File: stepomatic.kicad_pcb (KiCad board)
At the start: 2 copper layers, 50 x 30 mm, 31 parts, among them J1 I2C, J2 Conn_01x05, J4 USB_B_Micro, Q1 MMBT3904, Q2 MMBT3904, SW1 Mode, SW2 RST, U1 HDC1080DMBR, U2 AMS1117-3.3, U3 ULN2003A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

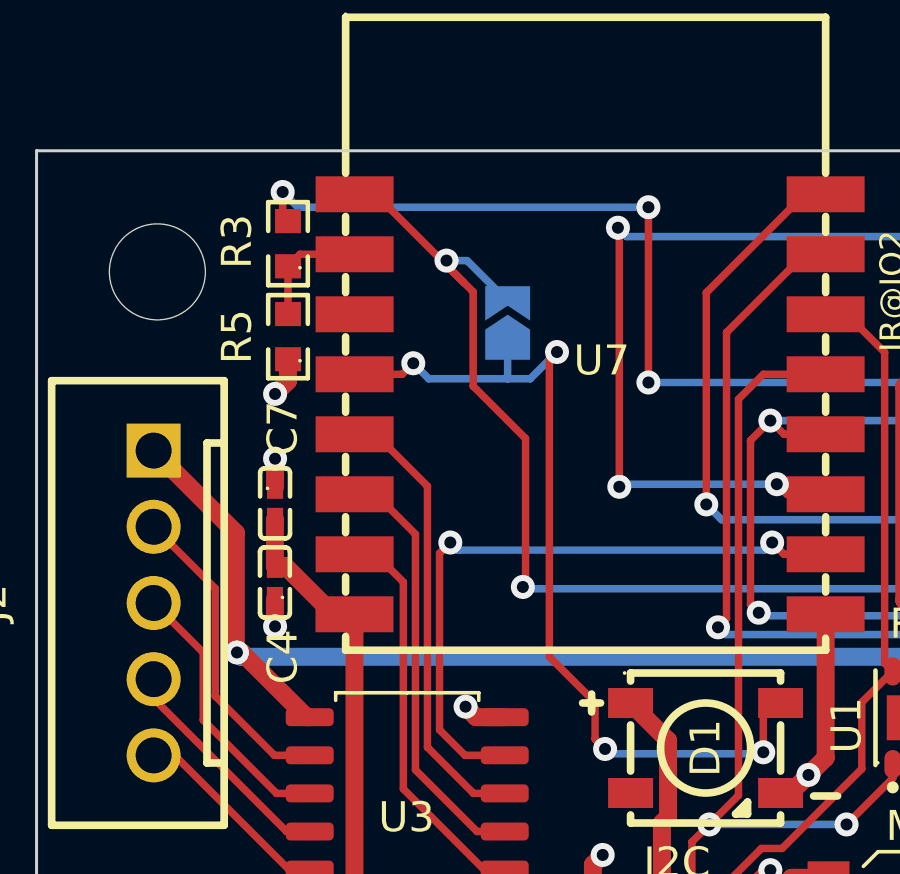
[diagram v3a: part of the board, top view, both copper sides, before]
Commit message: Fix package of C3
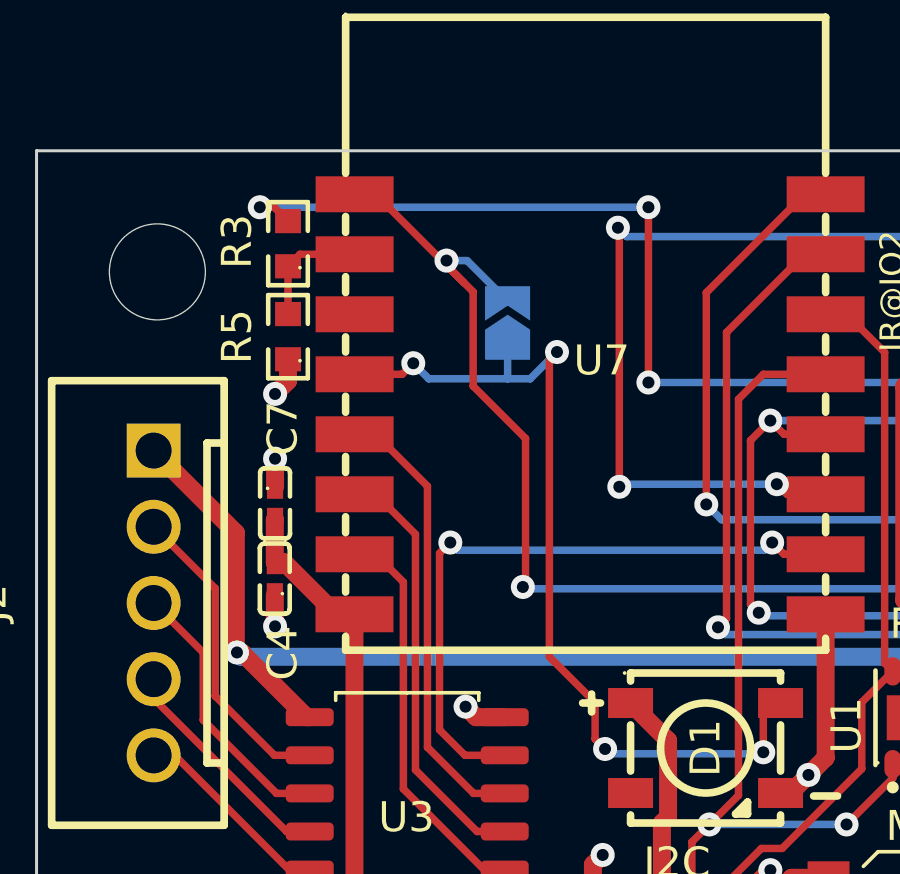
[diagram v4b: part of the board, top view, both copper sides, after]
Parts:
- moved C4 0.12 mm to (107.9, 84.3)
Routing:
- net Net-(CGQ1-Pad2): track 46.4 -> 47.1 mm
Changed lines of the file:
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@@
   )
   (footprint "footprint:C0402" (layer "F.Cu")
-    (at 107.94585 84.387329 90)
+    (at 107.941145 84.263232 90)
     (descr "C0402 footprint")
     (tags "C0402 footprint C1525")
@@
   (segment (start 141.475 86.8) (end 141.407 86.868) (width 0.6) (layer "B.Cu") (net 1))
   (segment (start 141.407 86.868) (end 106.824848 86.868) (width 0.6) (layer "B.Cu") (net 1))
-  (segment (start 107.94585 84.932414) (end 107.94585 85.84785) (width 0.6) (layer "F.Cu") (net 2))
   (segment (start 125.127358 91.407642) (end 125.73 90.805) (width 0.6) (layer "F.Cu") (net 2))
   (segment (start 133.33125 76.94325) (end 132.842 76.454) (width 0.6) (layer "F.Cu") (net 2))
@@
   (segment (start 132.6 94.234) (end 135.15 94.234) (width 0.6) (layer "F.Cu") (net 2))
   (segment (start 148.564985 78.627006) (end 148.564985 85.627006) (width 0.6) (layer "F.Cu") (net 2))
+  (segment (start 107.941145 84.808317) (end 107.941145 85.843145) (width 0.6) (layer "F.Cu") (net 2))
   (segment (start 143.346113 91.592136) (end 143.153977 91.4) (width 0.6) (layer "F.Cu") (net 2))
   (segment (start 141.35 94.234) (end 140.208 94.234) (width 0.6) (layer "F.Cu") (net 2))
@@
   (segment (start 145.864985 79.627006) (end 145.864985 80.677504) (width 0.6) (layer "F.Cu") (net 2))
   (segment (start 131.41617 76.454) (end 132.292049 76.454) (width 0.6) (layer "F.Cu") (net 2))
-  (segment (start 107.94585 85.84785) (end 107.95 85.852) (width 0.6) (layer "F.Cu") (net 2))
   (segment (start 124.145413 96.834587) (end 123.952 97.028) (width 0.6) (layer "F.Cu") (net 2))
   (segment (start 134.334912 92.072942) (end 133.982942 92.072942) (width 0.6) (layer "F.Cu") (net 2))
@@
   (segment (start 134.742562 83.95105) (end 134.611512 83.82) (width 0.6) (layer "F.Cu") (net 2))
   (segment (start 134.611512 83.82) (end 134.112 83.82) (width 0.6) (layer "F.Cu") (net 2))
+  (segment (start 107.941145 85.843145) (end 107.95 85.852) (width 0.6) (layer "F.Cu") (net 2))
   (segment (start 133.982942 92.072942) (end 133.604 91.694) (width 0.6) (layer "F.Cu") (net 2))
   (segment (start 107.95 81.20583) (end 107.95 80.264) (width 0.6) (layer "F.Cu") (net 2))
@@
   (segment (start 134.62 78.232) (end 134.742562 78.109438) (width 0.6) (layer "F.Cu") (net 3))
   (segment (start 130.221998 78.232) (end 134.62 78.232) (width 0.6) (layer "F.Cu") (net 3))
-  (segment (start 108.28865 83.842244) (end 107.94585 83.842244) (width 0.6) (layer "F.Cu") (net 3))
   (segment (start 138.552562 82.672562) (end 138.552562 83.95105) (width 0.6) (layer "F.Cu") (net 3))
   (segment (start 137.046113 89.292136) (end 136.145977 88.392) (width 0.6) (layer "F.Cu") (net 3))
   (segment (start 128.922606 84.982065) (end 128.922606 77.857394) (width 0.6) (layer "F.Cu") (net 3))
   (segment (start 121.05133 89.657896) (end 119.80133 88.407896) (width 0.6) (layer "F.Cu") (net 3))
+  (segment (start 108.254961 83.718147) (end 107.941145 83.718147) (width 0.6) (layer "F.Cu") (net 3))
   (segment (start 129.3 72.784822) (end 129.3 76.44) (width 0.6) (layer "F.Cu") (net 3))
   (segment (start 134.742562 79.00105) (end 134.742562 80.06477) (width 0.6) (layer "F.Cu") (net 3))
   (segment (start 129.82 76.96) (end 129.82 77.830002) (width 0.6) (layer "F.Cu") (net 3))
   (segment (start 134.42142 77.289542) (end 134.742562 77.610684) (width 0.6) (layer "F.Cu") (net 3))
+  (segment (start 107.941145 82.304855) (end 107.95 82.296) (width 0.6) (layer "F.Cu") (net 3))
+  (segment (start 110.596431 85.450025) (end 109.986839 85.450025) (width 0.6) (layer "F.Cu") (net 3))
   (segment (start 140.275826 74.920003) (end 140.275826 76.334216) (width 0.6) (layer "F.Cu") (net 3))
   (segment (start 120.845438 92.407642) (end 121.05133 92.20175) (width 0.6) (layer "F.Cu") (net 3))
@@
   (segment (start 137.16 99.06) (end 137.668 98.552) (width 0.6) (layer "F.Cu") (net 3))
   (segment (start 120.845438 98.857516) (end 121.047922 99.06) (width 0.6) (layer "F.Cu") (net 3))
-  (segment (start 110.596431 85.450025) (end 109.896431 85.450025) (width 0.6) (layer "F.Cu") (net 3))
-  (segment (start 107.94585 83.842244) (end 107.94585 82.30015) (width 0.6) (layer "F.Cu") (net 3))
+  (segment (start 107.941145 83.718147) (end 107.941145 82.304855) (width 0.6) (layer "F.Cu") (net 3))
   (segment (start 120.845438 97.78251) (end 120.845438 92.407642) (width 0.6) (layer "F.Cu") (net 3))
   (segment (start 140.275826 76.334216) (end 139.083992 77.52605) (width 0.6) (layer "F.Cu") (net 3))
@@
   (segment (start 115.175863 99.06) (end 121.412 99.06) (width 0.6) (layer "F.Cu") (net 3))
   (segment (start 134.742562 77.610684) (end 134.742562 78.109438) (width 0.6) (layer "F.Cu") (net 3))
-  (segment (start 107.94585 82.30015) (end 107.95 82.296) (width 0.6) (layer "F.Cu") (net 3))
   (segment (start 139.083992 77.52605) (end 135.32595 77.52605) (width 0.6) (layer "F.Cu") (net 3))
   (segment (start 134.742562 78.109438) (end 134.742562 78.62347) (width 0.6) (layer "F.Cu") (net 3))
   (segment (start 138.552562 83.95105) (end 138.552562 87.785687) (width 0.6) (layer "F.Cu") (net 3))
   (segment (start 137.668 98.552) (end 137.668 89.914023) (width 0.6) (layer "F.Cu") (net 3))
+  (segment (start 109.986839 85.450025) (end 108.254961 83.718147) (width 0.6) (layer "F.Cu") (net 3))
   (segment (start 110.596431 85.450025) (end 110.596431 94.480568) (width 0.6) (layer "F.Cu") (net 3))
   (segment (start 129.779565 72.305257) (end 129.3 72.784822) (width 0.6) (layer "F.Cu") (net 3))
-  (segment (start 109.896431 85.450025) (end 108.28865 83.842244) (width 0.6) (layer "F.Cu") (net 3))
   (segment (start 103.902943 82.533519) (end 105.9555 84.586076) (width 0.25) (layer "F.Cu") (net 4))
   (segment (start 107.930543 90.150543) (end 109.105645 90.150543) (width 0.25) (layer "F.Cu") (net 4))
@@
   (segment (start 131.078016 73.421984) (end 131.078016 72.305257) (width 0.25) (layer "F.Cu") (net 47))
   (segment (start 130.55 73.95) (end 131.078016 73.421984) (width 0.25) (layer "F.Cu") (net 47))
+  (segment (start 107.920324 71.882) (end 107.442 71.882) (width 0.25) (layer "F.Cu") (net 48))
   (segment (start 120.396 77.724) (end 120.396 71.882) (width 0.25) (layer "F.Cu") (net 48))
   (segment (start 140.275826 72.379997) (end 141.732 73.836171) (width 0.25) (layer "F.Cu") (net 48))
-  (segment (start 108.204 72.165676) (end 108.38176 72.343436) (width 0.25) (layer "F.Cu") (net 48))
   (segment (start 141.732 73.836171) (end 141.732 77.47) (width 0.25) (layer "F.Cu") (net 48))
-  (segment (start 108.204 71.374) (end 108.204 72.165676) (width 0.25) (layer "F.Cu") (net 48))
+  (segment (start 108.38176 72.343436) (end 107.920324 71.882) (width 0.25) (layer "F.Cu") (net 48))
   (via (at 141.732 77.47) (size 0.8) (drill 0.4) (layers "F.Cu" "B.Cu") (net 48))
   (via (at 120.396 71.882) (size 0.8) (drill 0.4) (layers "F.Cu" "B.Cu") (net 48))
-  (via (at 108.204 71.374) (size 0.8) (drill 0.4) (layers "F.Cu" "B.Cu") (net 48))
+  (via (at 107.442 71.882) (size 0.8) (drill 0.4) (layers "F.Cu" "B.Cu") (net 48))
   (via (at 120.396 77.724) (size 0.8) (drill 0.4) (layers "F.Cu" "B.Cu") (net 48))
-  (segment (start 108.712 71.882) (end 108.204 71.374) (width 0.25) (layer "B.Cu") (net 48))
   (segment (start 141.478 77.724) (end 141.732 77.47) (width 0.25) (layer "B.Cu") (net 48))
-  (segment (start 120.396 71.882) (end 108.712 71.882) (width 0.25) (layer "B.Cu") (net 48))
+  (segment (start 120.396 71.882) (end 107.442 71.882) (width 0.25) (layer "B.Cu") (net 48))
   (segment (start 120.396 77.724) (end 141.478 77.724) (width 0.25) (layer "B.Cu") (net 48))
   (zone (net 3) (net_name "+3V3") (layer "F.Cu") (hatch edge 0.508)

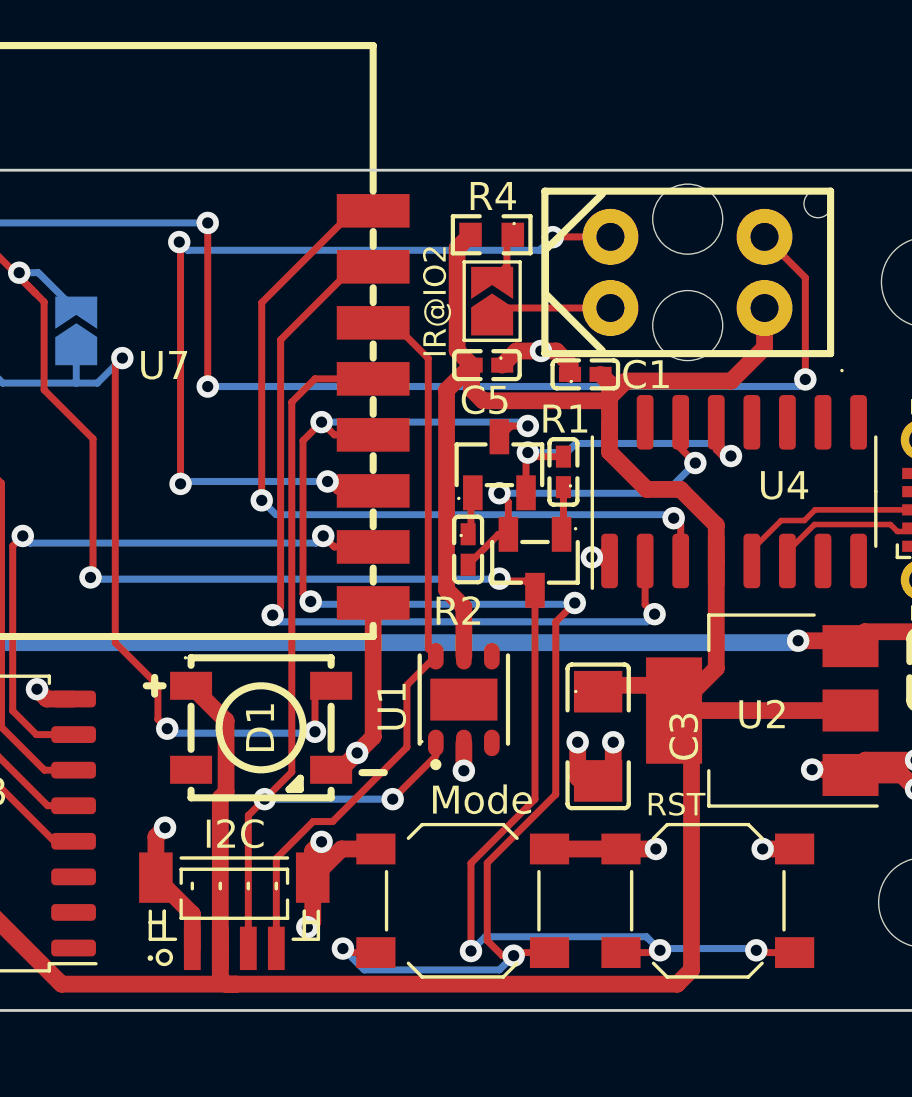
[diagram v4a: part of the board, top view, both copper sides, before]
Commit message: Allow to switch between ON and GPIO02 for IR send
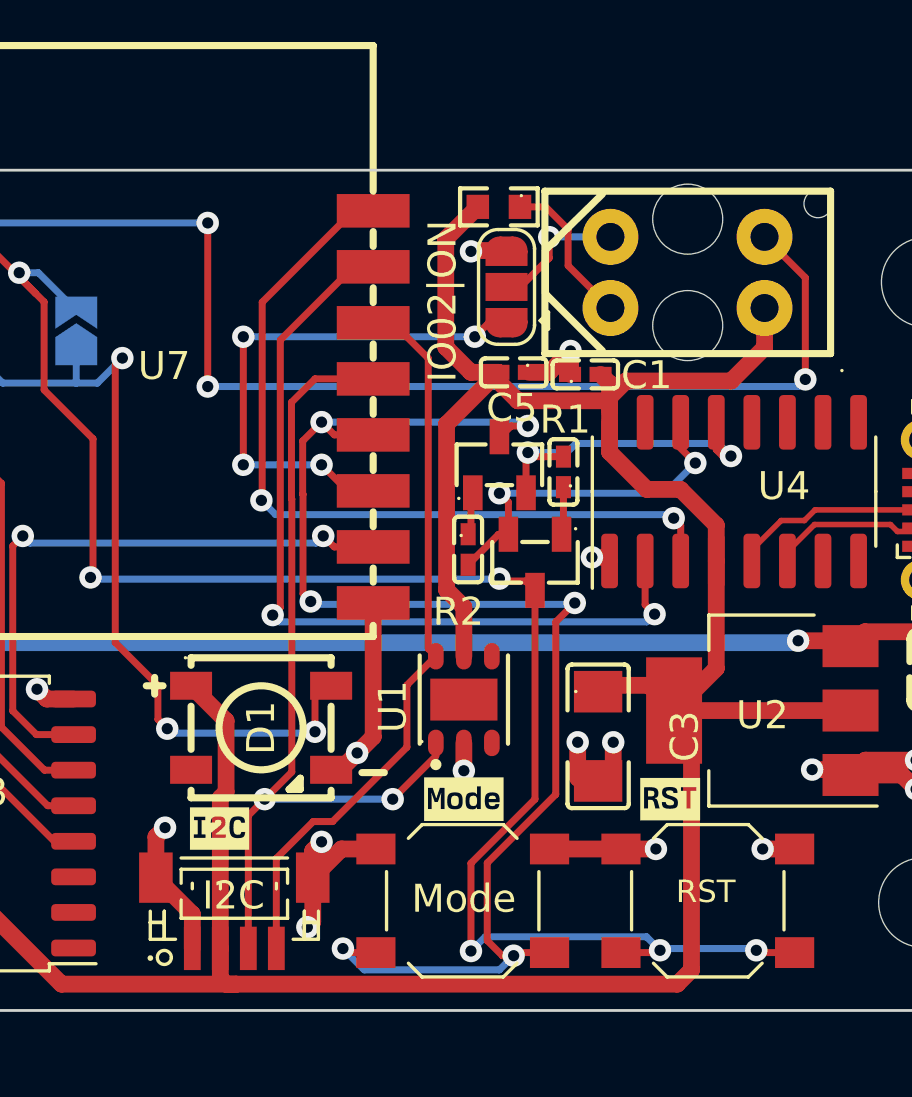
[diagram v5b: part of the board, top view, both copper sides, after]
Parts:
- added kibuzzard-65CA9226: G***, kibuzzard-65CA9226, F.Cu at (120.8, 93.5)
- added kibuzzard-65CA923B: G***, kibuzzard-65CA923B, F.Cu at (129.5, 92.5)
- added kibuzzard-65CA9256: G***, kibuzzard-65CA9256, F.Cu at (136.9, 92.5)
- JP2: value IR@IO2 -> IO02|ON; footprint Jumper:SolderJumper-2_P1.3mm_Open_TrianglePad1.0x1.5mm -> Jumper:SolderJumper-3_P1.3mm_Open_RoundedPad1.0x1.5mm
- moved R4 1.03 mm to (130.8, 71.3)
- moved C5 0.99 mm to (131.3, 77.2)
- moved JP2 0.72 mm to (131.1, 74.2)
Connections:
- CGQ1 pad 4: IR -> Net-(CGQ1-Pad4)
- JP2 pad 1: Net-(CGQ1-Pad3) -> IR
- JP2 pad 2: Net-(JP2-Pad2) -> Net-(CGQ1-Pad4)
- R4 pad 1: Net-(JP2-Pad2) -> Net-(CGQ1-Pad3)
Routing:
- net IR: track 31.4 -> 19.2 mm
- net Net-(CGQ1-Pad4): track 0.00 -> 4.89 mm, vias 0 -> 1
- net Net-(JP2-Pad2): track 1.86 -> 0.00 mm
- net +3V3: track 117.4 -> 118.8 mm
- net Net-(CGQ1-Pad3): track 4.42 -> 5.49 mm
- net GND: track 52.2 -> 53.0 mm, vias 19 -> 20
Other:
- board text added: "JLCJLCJLCJLC"

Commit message: Tidy up
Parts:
- added kibuzzard-65CA9AB8: G***, kibuzzard-65CA9AB8, F.Cu at (128.8, 74.4)
- added kibuzzard-65CA9B57: G***, kibuzzard-65CA9B57, F.Cu at (105.7, 76.7)
- added kibuzzard-65CA9BC7: G***, kibuzzard-65CA9BC7, B.Cu at (111.5, 75.7)
- added kibuzzard-65CA9C5F: G***, kibuzzard-65CA9C5F, F.Cu at (119.9, 99.1)
- added kibuzzard-65CA9C8E: G***, kibuzzard-65CA9C8E, F.Cu at (121.0, 99.1)
- added kibuzzard-65CA9CFD: G***, kibuzzard-65CA9CFD, F.Cu at (123.0, 99.1)
- added kibuzzard-65CA9D0A: G***, kibuzzard-65CA9D0A, F.Cu at (122.0, 99.1)
- added kibuzzard-65CA9D34: G***, kibuzzard-65CA9D34, F.Cu at (148.6, 88.4)
- added kibuzzard-65CA9DAF: G***, kibuzzard-65CA9DAF, F.Cu at (103.4, 93.3)
- J2: value Conn_01x05 -> 28BYJ-48
- JP2: value IO02|ON -> IR
- moved kibuzzard-65CA9256 0.76 mm to (137.7, 92.5)
- moved U2 0.70 mm to (140.8, 89.0)
- moved kibuzzard-65CA9226 0.59 mm to (121.4, 93.6)
- moved U1 0.51 mm to (130.0, 88.9)
- moved C7 0.44 mm to (108.0, 81.3)
- moved C4 0.44 mm to (108.0, 83.8)
- moved J1 0.15 mm to (121.5, 96.5)
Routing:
- net +3V3: track 118.8 -> 129.1 mm
- net IR: track 19.2 -> 22.2 mm
- net GPIO16: track 29.9 -> 28.0 mm
- net RTS: track 12.7 -> 14.1 mm
- net TX: track 28.3 -> 29.6 mm
- net GND: track 53.0 -> 51.8 mm
- net STEPPER4: track 21.8 -> 21.0 mm
- net RESET: track 62.9 -> 63.4 mm
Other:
- board text removed: "THE CURRENT IS TOO HIGH @ 150Ohm only 12mA are allowed"

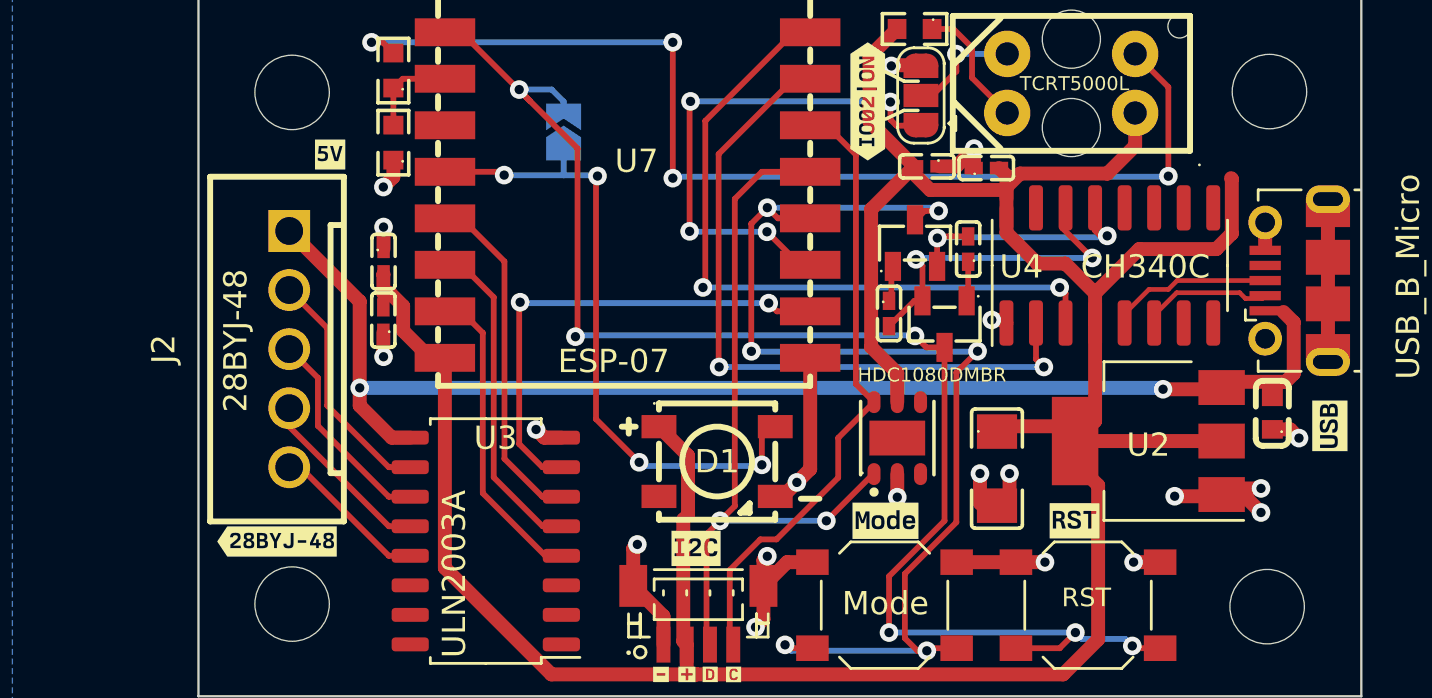
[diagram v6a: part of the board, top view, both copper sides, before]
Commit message: Fix orientation of the stepper motor plug
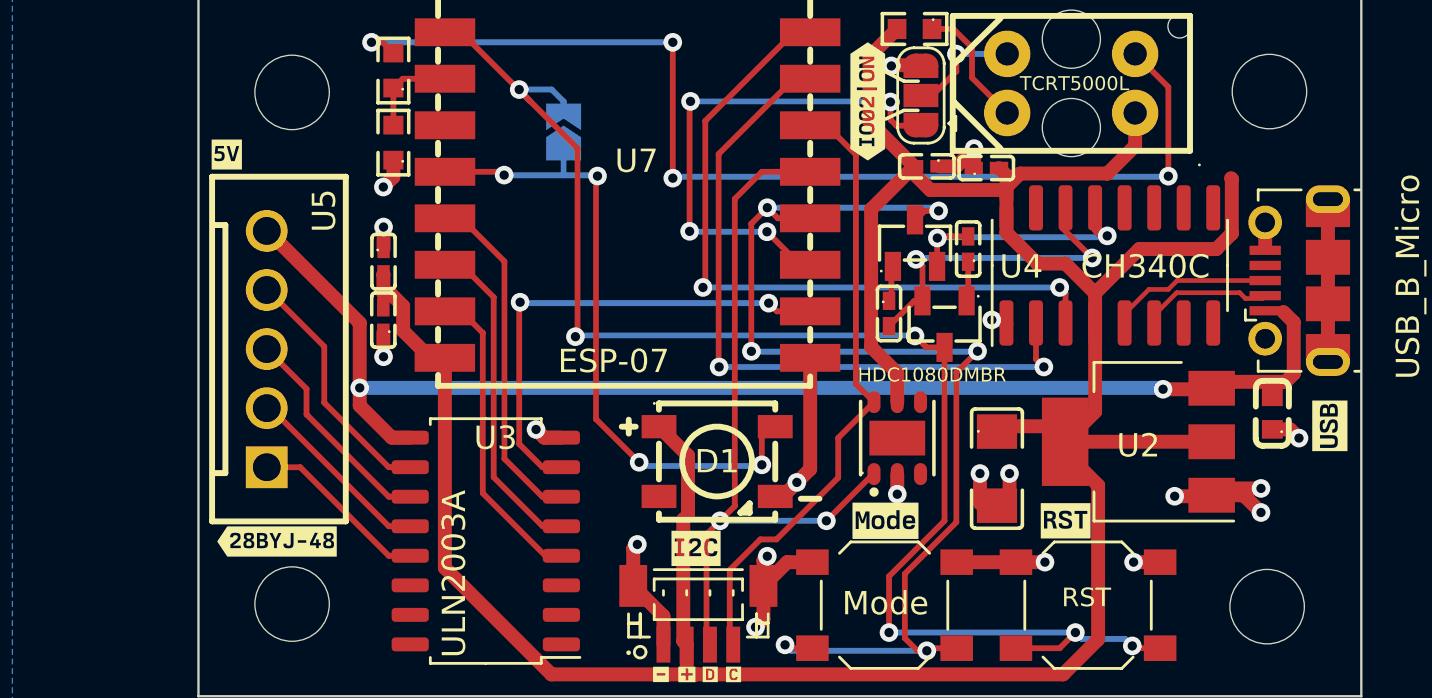
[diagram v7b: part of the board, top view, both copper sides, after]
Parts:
- removed J2: 28BYJ-48, footprint:CONN-TH_B5B-XH-A-LF-SN
- added U5: 28BYJ-48, footprint:CONN-TH_B5B-XH-A-LF-SN, F.Cu at (102.9, 85.1)
- C2: value CL10A226MQ8NRNC -> 22u
- moved kibuzzard-65CA9B57 4.45 mm to (101.2, 76.7)
- moved U2 0.43 mm to (140.4, 89.1)
- moved kibuzzard-65CA9256 0.38 mm to (137.3, 92.5)
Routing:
- net Net-(U3-Pad13): track 6.78 -> 7.75 mm
- net Net-(U3-Pad12): track 7.77 -> 8.27 mm
